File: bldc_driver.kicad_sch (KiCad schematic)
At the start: 5 parts, among them U1 AS5048A, U2 STM32G0B1KCTx, U3 SN65HVD230, U4 UA78M33QDCYRQ1, U5 DRV8317HREER

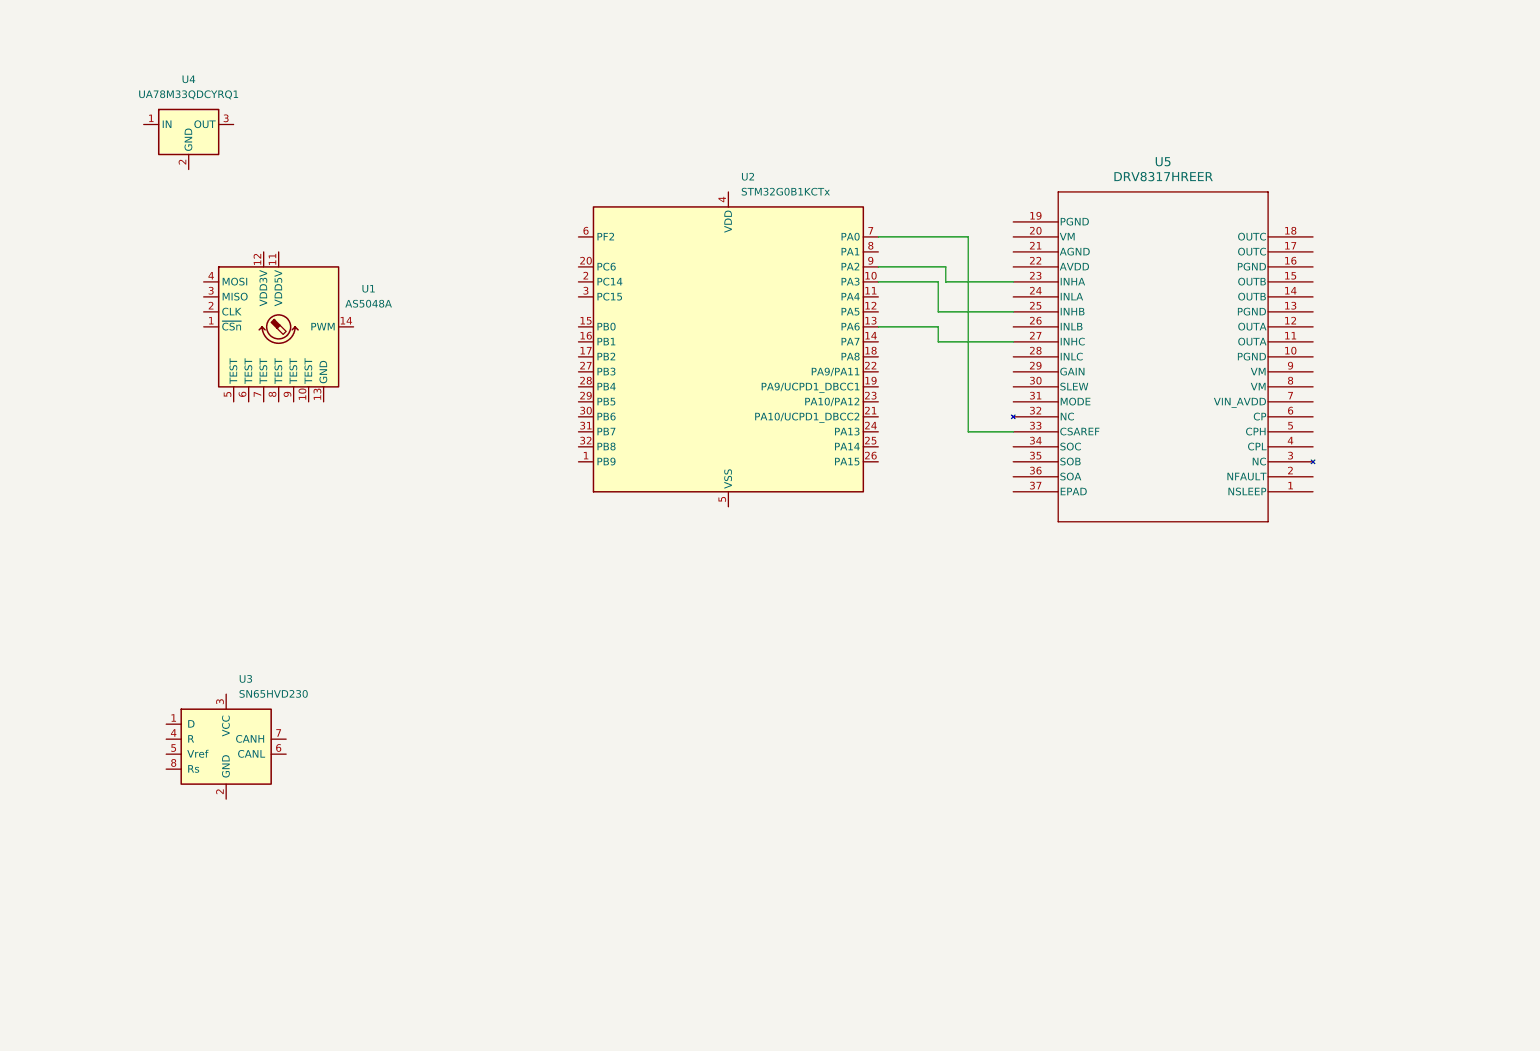
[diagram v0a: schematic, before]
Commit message: progress on schematic for DRV8317H
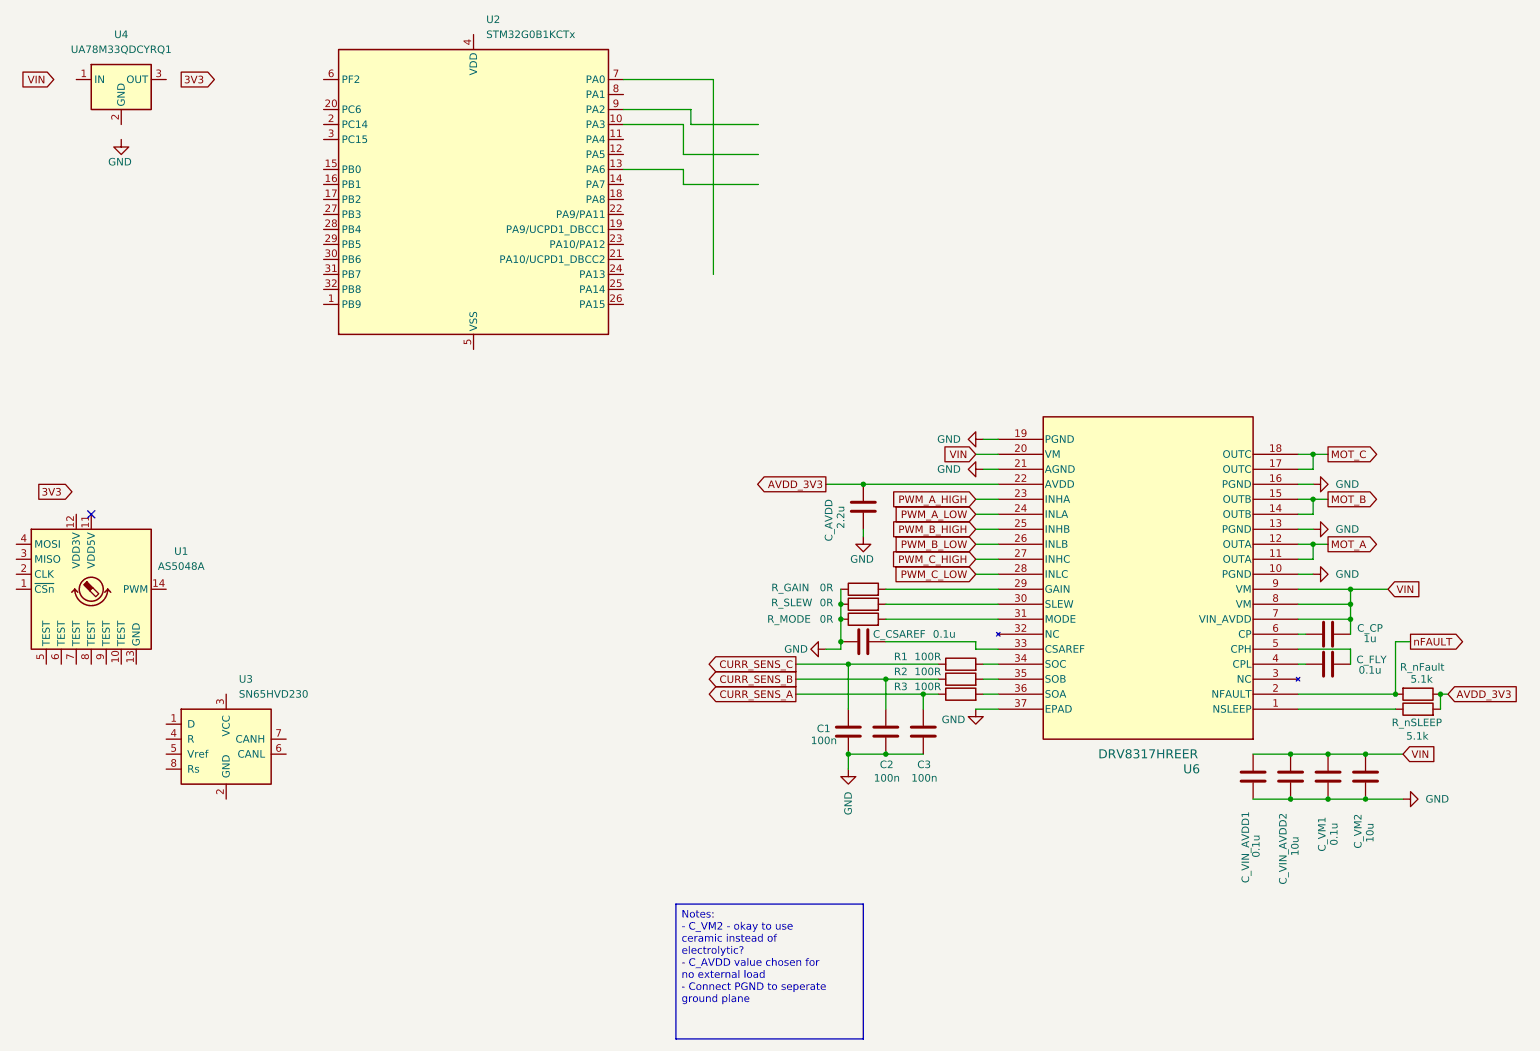
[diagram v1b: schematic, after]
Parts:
- removed U5: DRV8317HREER, WQFN36_REE_TEX, symbol 2025-04-23_22-21-06:DRV8317HREER
- added C1, C2, C3: 100n, Capacitor_SMD:C_0402_1005Metric_Pad0.74x0.62mm_HandSolder, symbol Device:C
- added C_AVDD: 2.2u, symbol Device:C
- added C_CP: 1u, symbol Device:C
- added C_CSAREF, C_FLY, C_VIN_AVDD1, C_VM1: 0.1u, symbol Device:C
- added C_VIN_AVDD2, C_VM2: 10u, symbol Device:C
- added R1, R2, R3: 100R, Resistor_SMD:R_0402_1005Metric_Pad0.72x0.64mm_HandSolder, symbol Device:R
- added R_GAIN, R_SLEW: 0R, symbol Device:R
- added R_MODE: 0R, Resistor_SMD:R_0603_1608Metric_Pad0.98x0.95mm_HandSolder, symbol Device:R
- added R_nFault, R_nSLEEP: 5.1k, symbol Device:R
- added U6: DRV8317HREER, WQFN36_REE_TEX, symbol bldc_driver_lib:DRV8317HREER
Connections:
- new net: R_MODE.2, U6.31 (MODE)
- new net: R2.2, U6.35 (SOB)
- new net: R_nSLEEP.1, U6.1 (NSLEEP)
- new net: R_SLEW.2, U6.30 (SLEW)
- new net: C_CP.1, U6.6 (CP)
- new net: R3.2, U6.36 (SOA)
- new net: R_GAIN.2, U6.29 (GAIN)
- new net: C_CSAREF.2, U6.33 (CSAREF)
- new net: R1.2, U6.34 (SOC)
- new net: C_FLY.1, U6.4 (CPL)
- new net: C_FLY.2, U6.5 (CPH)
- new net AVDD_3V3: C_AVDD.2, R_nFault.1, R_nSLEEP.2, U6.22 (AVDD)
- new net CURR_SENS_A: C3.1, R3.1
- new net CURR_SENS_B: C2.1, R2.1
- new net CURR_SENS_C: C1.1, R1.1
- new net GND: C1.2, C2.2, C3.2, C_AVDD.1, C_CSAREF.1, C_VIN_AVDD1.2, C_VIN_AVDD2.1, C_VM1.2, C_VM2.2, R_GAIN.1, R_MODE.1, R_SLEW.1, U6.10 (PGND), U6.13 (PGND), U6.16 (PGND), U6.19 (PGND), U6.21 (AGND), U6.37 (EPAD)
- new net MOT_A: U6.11 (OUTA), U6.12 (OUTA)
- new net MOT_B: U6.14 (OUTB), U6.15 (OUTB)
- new net MOT_C: U6.17 (OUTC), U6.18 (OUTC)
- new net PWM_A_HIGH: U6.23 (INHA)
- new net PWM_A_LOW: U6.24 (INLA)
- new net PWM_B_HIGH: U6.25 (INHB)
- new net PWM_B_LOW: U6.26 (INLB)
- new net PWM_C_HIGH: U6.27 (INHC)
- new net PWM_C_LOW: U6.28 (INLC)
- new net VIN: C_CP.2, C_VIN_AVDD1.1, C_VIN_AVDD2.2, C_VM1.1, C_VM2.1, U6.20 (VM), U6.7 (VIN_AVDD), U6.8 (VM), U6.9 (VM)
- new net nFAULT: R_nFault.2, U6.2 (NFAULT)
- no-connect marks 0 -> 1
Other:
- moved on the sheet: U1, U2, U4

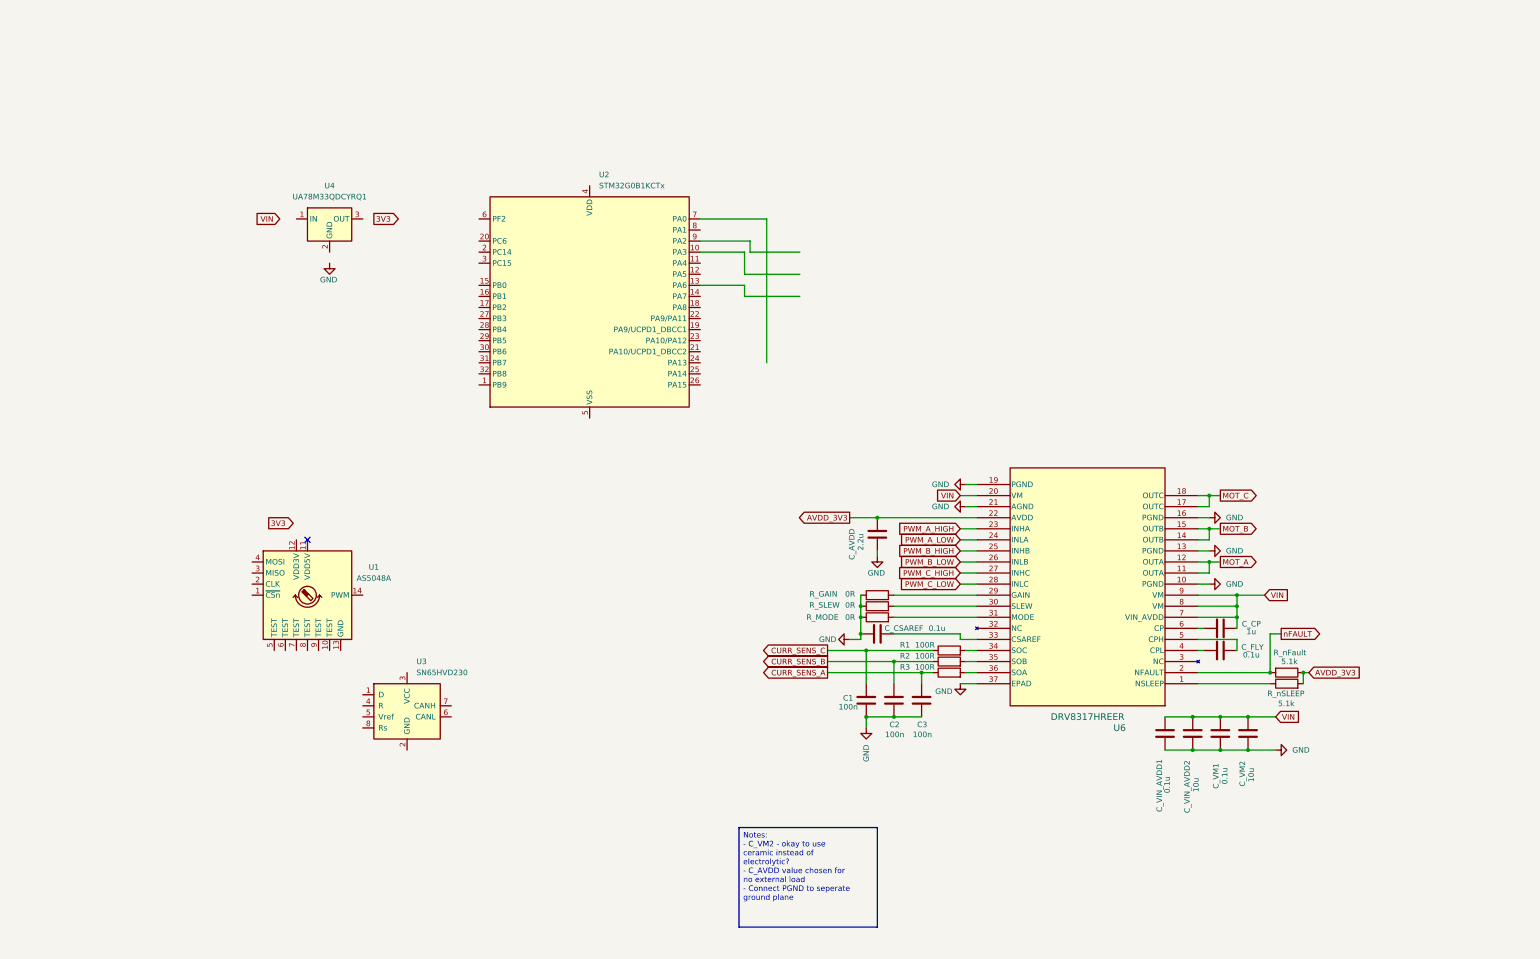
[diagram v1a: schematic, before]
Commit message: initial placement of componeents
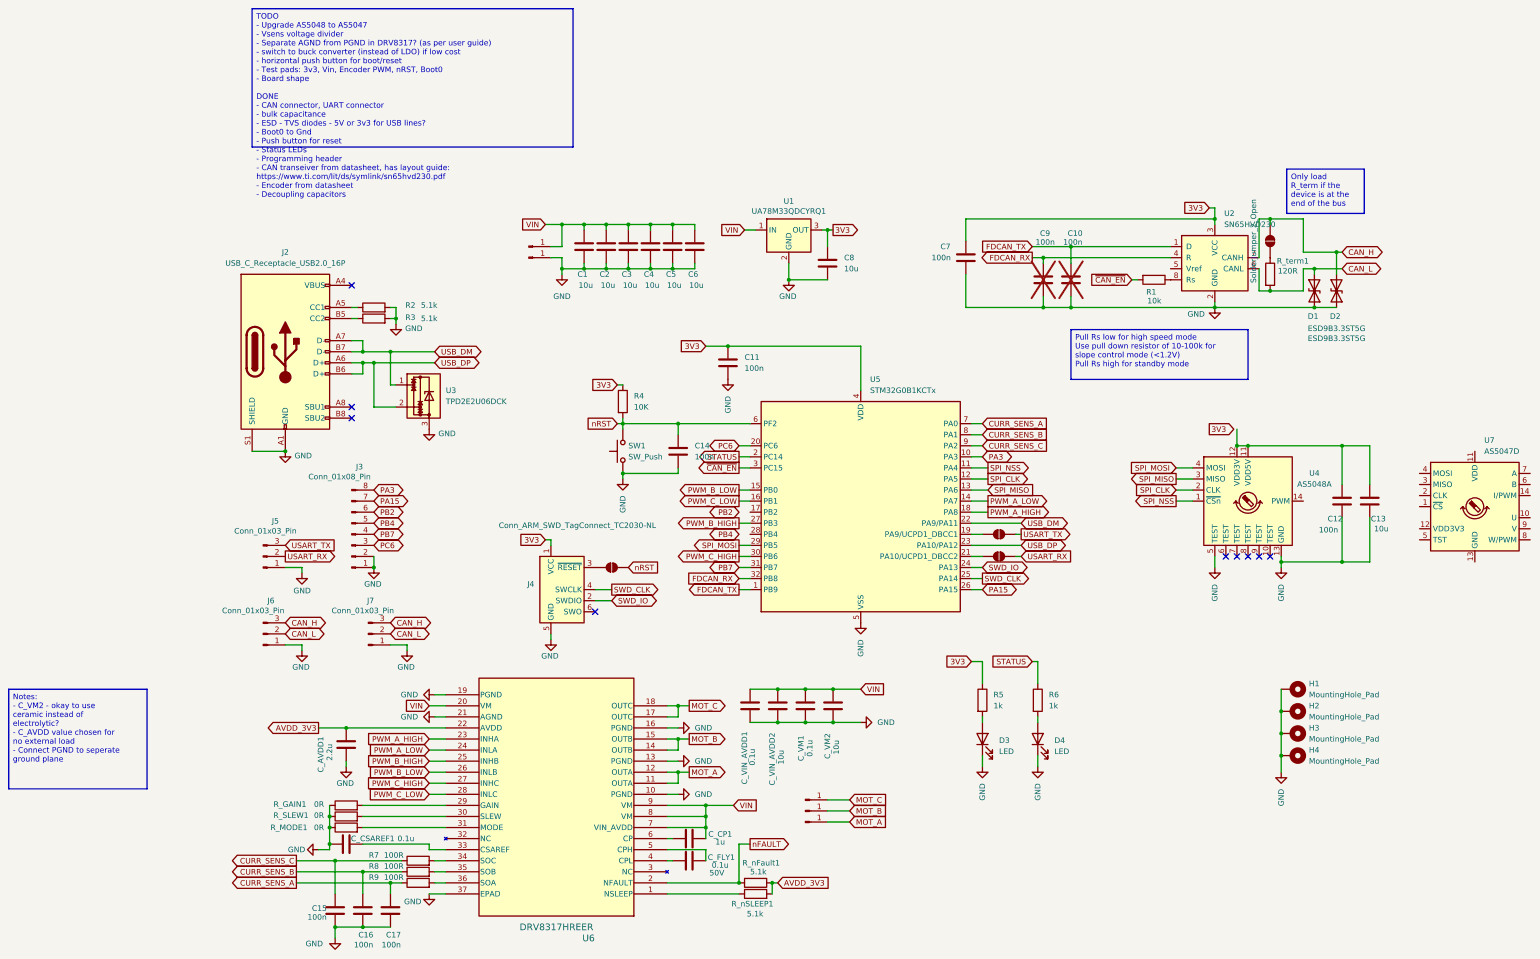
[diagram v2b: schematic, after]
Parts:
- removed U3: SN65HVD230, Package_SO:SOIC-8_3.9x4.9mm_P1.27mm, symbol Interface_CAN_LIN:SN65HVD230
- added C1, C2, C3, C4, C5, C6, C8: 10u, Capacitor_SMD:C_1210_3225Metric_Pad1.33x2.70mm_HandSolder, symbol Device:C
- added C10, C12, C14, C7, C9: 100n, Capacitor_SMD:C_0402_1005Metric_Pad0.74x0.62mm_HandSolder, symbol Device:C
- added C11: 100n, Capacitor_SMD:C_0603_1608Metric_Pad1.08x0.95mm_HandSolder, symbol Device:C
- added C13: 10u, Capacitor_SMD:C_0603_1608Metric_Pad1.08x0.95mm_HandSolder, symbol Device:C
- added D1, D2: ESD9B3.3ST5G, Diode_SMD:D_SOD-923, symbol Diode:ESD9B3.3ST5G
- added D3, D4: LED, LED_SMD:LED_0402_1005Metric_Pad0.77x0.64mm_HandSolder, symbol Device:LED
- added H1, H2, H3, H4: MountingHole_Pad, MountingHole:MountingHole_2.7mm_M2.5_DIN965_Pad_TopBottom, symbol Mechanical:MountingHole_Pad
- added J1, J10, J11, J8, J9: Conn_01x01_Pin, Connector_Wire:SolderWire-0.75sqmm_1x01_D1.25mm_OD3.5mm, symbol Connector:Conn_01x01_Pin
- added J2: USB_C_Receptacle_USB2.0_16P, Connector_USB:USB_C_Receptacle_GCT_USB4110, symbol Connector:USB_C_Receptacle_USB2.0_16P
- added J3: Conn_01x08_Pin, Connector_PinHeader_2.54mm:PinHeader_2x04_P2.54mm_Vertical, symbol Connector:Conn_01x08_Pin
- added J4: Conn_ARM_SWD_TagConnect_TC2030-NL, Connector:Tag-Connect_TC2030-IDC-NL_2x03_P1.27mm_Vertical, symbol Connector:Conn_ARM_SWD_TagConnect_TC2030-NL
- added J5: Conn_01x03_Pin, Connector_PinHeader_2.54mm:PinHeader_1x03_P2.54mm_Vertical, symbol Connector:Conn_01x03_Pin
- added J6, J7: Conn_01x03_Pin, Connector_PinSocket_2.54mm:PinSocket_1x03_P2.54mm_Vertical, symbol Connector:Conn_01x03_Pin
- added JP1, JP2, JP3, JP4: SolderJumper_2_Open, Jumper:SolderJumper-2_P1.3mm_Open_TrianglePad1.0x1.5mm, symbol Jumper:SolderJumper_2_Open
- added R1: 10k, Resistor_SMD:R_0402_1005Metric_Pad0.72x0.64mm_HandSolder, symbol Device:R
- added R2, R3: 5.1k, Resistor_SMD:R_0402_1005Metric_Pad0.72x0.64mm_HandSolder, symbol Device:R
- added R4: 10K, Resistor_SMD:R_0402_1005Metric_Pad0.72x0.64mm_HandSolder, symbol Device:R
- added R5, R6: 1k, Resistor_SMD:R_0402_1005Metric_Pad0.72x0.64mm_HandSolder, symbol Device:R
- added R_term1: 120R, Resistor_SMD:R_0201_0603Metric_Pad0.64x0.40mm_HandSolder, symbol Device:R
- added SW1: SW_Push, Button_Switch_SMD:SW_Tactile_SPST_NO_Straight_CK_PTS636Sx25SMTRLFS, symbol Switch:SW_Push
- added U2: SN65HVD230, Package_SO:SOIC-8_3.9x4.9mm_P1.27mm, symbol Interface_CAN_LIN:SN65HVD230
- added U3: TPD2E2U06DCK, Package_TO_SOT_SMD:SOT-323_SC-70, symbol Power_Protection:TPD2E2U06DCK
- added U7: AS5047D, Package_SO:TSSOP-14_4.4x5mm_P0.65mm, symbol Sensor_Magnetic:AS5047D
- C_AVDD1: renamed from C_AVDD; footprint (none) -> Capacitor_SMD:C_0603_1608Metric_Pad1.08x0.95mm_HandSolder
- C_CP1: renamed from C_CP; footprint (none) -> Capacitor_SMD:C_0402_1005Metric_Pad0.74x0.62mm_HandSolder
- C_CSAREF1: renamed from C_CSAREF; footprint (none) -> Capacitor_SMD:C_0402_1005Metric_Pad0.74x0.62mm_HandSolder
- C_FLY1: renamed from C_FLY; footprint (none) -> Capacitor_SMD:C_0402_1005Metric_Pad0.74x0.62mm_HandSolder; Rating (none) -> 50V
- C_VIN_AVDD1, C_VM1: footprint (none) -> Capacitor_SMD:C_0402_1005Metric_Pad0.74x0.62mm_HandSolder
- C_VIN_AVDD2, C_VM2: footprint (none) -> Capacitor_SMD:C_0603_1608Metric_Pad1.08x0.95mm_HandSolder
- R_GAIN1: renamed from R_GAIN; footprint (none) -> Resistor_SMD:R_0402_1005Metric_Pad0.72x0.64mm_HandSolder
- R_MODE1: renamed from R_MODE; footprint Resistor_SMD:R_0603_1608Metric_Pad0.98x0.95mm_HandSolder -> Resistor_SMD:R_0402_1005Metric_Pad0.72x0.64mm_HandSolder
- R_SLEW1: renamed from R_SLEW; footprint (none) -> Resistor_SMD:R_0402_1005Metric_Pad0.72x0.64mm_HandSolder
- R_nFault1: renamed from R_nFault; footprint (none) -> Resistor_SMD:R_0402_1005Metric_Pad0.72x0.64mm_HandSolder
- R_nSLEEP1: renamed from R_nSLEEP; footprint (none) -> Resistor_SMD:R_0402_1005Metric_Pad0.72x0.64mm_HandSolder
- renumbered C1 to C15, C2 to C16, C3 to C17, R1 to R7, R2 to R8, R3 to R9, U4 to U1, U1 to U4, U2 to U5
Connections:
- net 3V3: now also U1.3 (OUT), U5.4 (VDD), C11.1, C7.1, C8.1, J4.1 (VCC), R4.1, R5.1, U2.3 (VCC)
- net CURR_SENS_A: now also U5.7 (PA0)
- net CURR_SENS_B: now also U5.8 (PA1)
- net CURR_SENS_C: now also U5.9 (PA2)
- net GND: now also U1.2 (GND), U4.13 (GND), U4.5 (TEST), U5.5 (VSS), C1.2, C10.2, C11.2, C12.2, C13.2, C14.2, C2.2, C3.2, C4.2, C5.2, C6.2, C7.2, C8.2, C9.2, D1.1 (A1), D2.1 (A1), D3.1 (K), D4.1 (K), H1.1, H2.1, H3.1, H4.1, J1.1 (Pin_1), J2.A1 (GND), J2.A12 (GND), J2.B1 (GND), J2.B12 (GND), J2.S1 (SHIELD), J3.1 (Pin_1), J3.2 (Pin_2), J4.5 (GND), J5.1 (Pin_1), J6.1 (Pin_1), J7.1 (Pin_1), R2.2, R3.2, SW1.1, U2.2 (GND), U3.3
- net MOT_A: now also J8.1 (Pin_1)
- net MOT_B: now also J9.1 (Pin_1)
- net MOT_C: now also J10.1 (Pin_1)
- net PWM_A_HIGH: now also U5.18 (PA8)
- net PWM_A_LOW: now also U5.14 (PA7)
- net PWM_B_HIGH: now also U5.27 (PB3)
- net PWM_B_LOW: now also U5.15 (PB0)
- net PWM_C_HIGH: now also U5.30 (PB6)
- net PWM_C_LOW: now also U5.16 (PB1)
- net VIN: now also U1.1 (IN), C1.1, C2.1, C3.1, C4.1, C5.1, C6.1, J11.1 (Pin_1)
- net FDCAN_TX: now reaches U5.1 (PB9)
- net FDCAN_TX: now also C10.1, U2.1 (D)
- net PA3: now reaches U5.10 (PA3)
- net PA3: now also J3.8 (Pin_8)
- net SPI_NSS: now reaches U5.11 (PA4)
- net SPI_NSS: now also U4.1 (~{CSn})
- net SPI_CLK: now reaches U5.12 (PA5)
- net SPI_CLK: now also U4.2 (CLK)
- net SPI_MISO: now reaches U5.13 (PA6)
- net SPI_MISO: now also U4.3 (MISO)
- net at U5.19 (PA9/UCPD1_DBCC1): now also JP3.1 (A)
- net STATUS: now reaches U5.2 (PC14)
- net STATUS: now also R6.1
- net PC6: now reaches U5.20 (PC6)
- net PC6: now also J3.3 (Pin_3)
- net at U5.21 (PA10/UCPD1_DBCC2): now also JP4.1 (A)
- net USB_DM: now reaches U5.22 (PA9/PA11)
- net USB_DM: now also J2.A7 (D-), J2.B7 (D-), U3.1
- net USB_DP: now reaches U5.23 (PA10/PA12)
- net USB_DP: now also J2.A6 (D+), J2.B6 (D+), U3.2
- net SWD_IO: now reaches U5.24 (PA13)
- net SWD_IO: now also J4.2 (SWDIO)
- net SWD_CLK: now reaches U5.25 (PA14)
- net SWD_CLK: now also J4.4 (SWCLK)
- net PA15: now reaches U5.26 (PA15)
- net PA15: now also J3.7 (Pin_7)
- net SPI_MOSI: now reaches U5.29 (PB5)
- net SPI_MOSI: now also U4.4 (MOSI)
- net ~{CAN_EN}: now reaches U5.3 (PC15)
- net ~{CAN_EN}: now also R1.2
- net PB7: now reaches U5.31 (PB7)
- net PB7: now also J3.4 (Pin_4)
- net FDCAN_RX: now reaches U5.32 (PB8)
- net FDCAN_RX: now also C9.1, U2.4 (R)
- net nRST: now reaches U5.6 (PF2)
- net nRST: now also C14.1, JP2.2 (B), R4.2, SW1.2
- net at U4.11 (VDD5V): now also U4.12 (VDD3V), C12.1, C13.1
- new net: D3.2 (A), R5.2
- new net: JP1.1 (A), R_term1.1
- new net: J2.A4 (VBUS), J2.A9 (VBUS), J2.B4 (VBUS), J2.B9 (VBUS)
- new net: J2.A5 (CC1), R2.1
- new net: J2.B5 (CC2), R3.1
- new net: D4.2 (A), R6.2
- new net: J4.3 (~{RESET}), JP2.1 (A)
- new net: R1.1, U2.8 (Rs)
- new net CAN_H: D2.2 (A2), J6.3 (Pin_3), J7.3 (Pin_3), JP1.2 (B), U2.7 (CANH)
- new net CAN_L: D1.2 (A2), J6.2 (Pin_2), J7.2 (Pin_2), R_term1.2, U2.6 (CANL)
- new net PB2: J3.6 (Pin_6)
- new net PB4: J3.5 (Pin_5)
- new net USART_RX: J5.2 (Pin_2), JP4.2 (B)
- new net USART_TX: J5.3 (Pin_3), JP3.2 (B)
- no-connect marks 1 -> 9
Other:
- moved on the sheet: C15, C16, C17, C_AVDD1, C_CP1, C_CSAREF1, C_FLY1, C_VIN_AVDD1, C_VIN_AVDD2, C_VM1, C_VM2, R7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
